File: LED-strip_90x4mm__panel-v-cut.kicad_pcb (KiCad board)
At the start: 2 copper layers, 99 x 100 mm, 774 parts, among them P1 CONN_2, P10 CONN_2, P11 CONN_2, P12 CONN_2, P2 CONN_2, P3 CONN_2, P4 CONN_2, P5 CONN_2, P6 CONN_2, P7 CONN_2, P8 CONN_2, P9 CONN_2

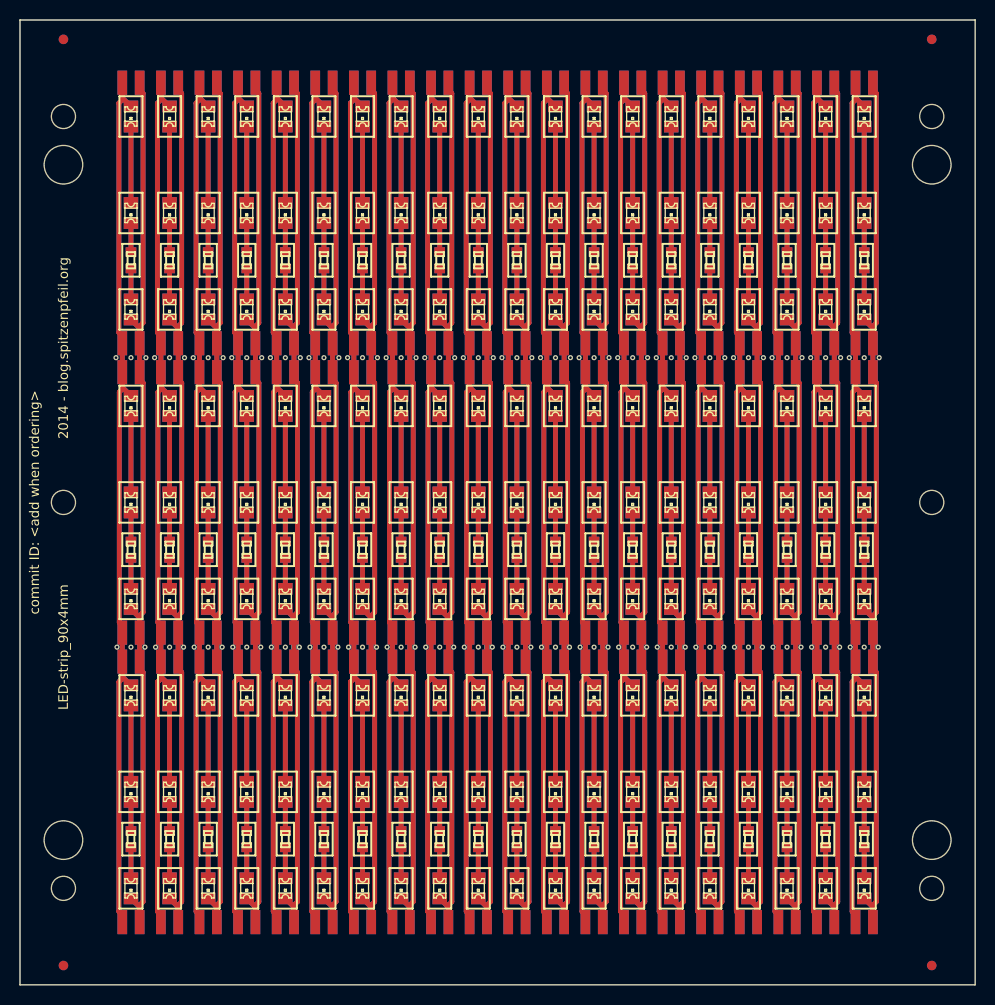
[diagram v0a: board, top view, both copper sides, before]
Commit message: Removed fiducials + alignment holes from panel --> 20% more boards.
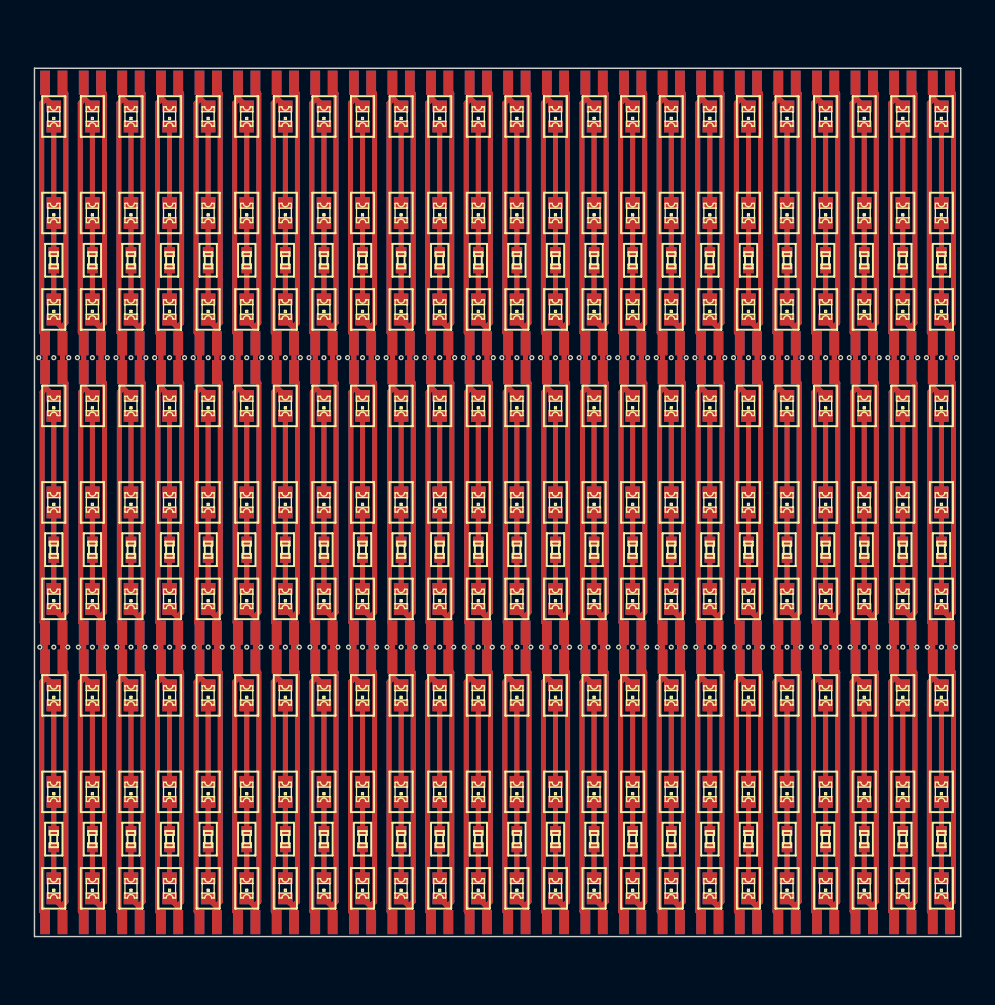
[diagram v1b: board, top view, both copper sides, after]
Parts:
- removed 1PIN (x4): P***, 1pin
- removed BH1: BH1, 1pin
- removed BH2: BH2, 1pin
- removed BH3: BH3, 1pin
- removed BH4: BH4, 1pin
- removed SM1: SM1, 1pin
- removed SM2: SM2, 1pin
- removed SM3: SM3, 1pin
- removed SM4: SM4, 1pin
- removed SM5: SM5, 1pin
- removed SM6: SM6, 1pin
- added D1: LED, my_parts:MADW__CHIPLED-0805, F.Cu at (288.5, 153.0)
- added D1: LED, my_parts:MADW__CHIPLED-0805, F.Cu at (284.5, 153.0)
- added D1: LED, my_parts:MADW__CHIPLED-0805, F.Cu at (372.5, 153.0)
- added D1: LED, my_parts:MADW__CHIPLED-0805, F.Cu at (376.5, 153.0)
- added D10: LED, my_parts:MADW__CHIPLED-0805, B.Cu at (288.5, 93.0)
- added D10: LED, my_parts:MADW__CHIPLED-0805, B.Cu at (284.5, 93.0)
- added D10: LED, my_parts:MADW__CHIPLED-0805, B.Cu at (372.5, 93.0)
- added D10: LED, my_parts:MADW__CHIPLED-0805, B.Cu at (376.5, 93.0)
- added D11: LED, my_parts:MADW__CHIPLED-0805, B.Cu at (288.5, 103.0)
- added D11: LED, my_parts:MADW__CHIPLED-0805, B.Cu at (284.5, 103.0)
- added D11: LED, my_parts:MADW__CHIPLED-0805, B.Cu at (372.5, 103.0)
- added D11: LED, my_parts:MADW__CHIPLED-0805, B.Cu at (376.5, 103.0)
- added D12: LED, my_parts:MADW__CHIPLED-0805, B.Cu at (288.5, 113.0)
- added D12: LED, my_parts:MADW__CHIPLED-0805, B.Cu at (284.5, 113.0)
- added D12: LED, my_parts:MADW__CHIPLED-0805, B.Cu at (372.5, 113.0)
- added D12: LED, my_parts:MADW__CHIPLED-0805, B.Cu at (376.5, 113.0)
- added D13: LED, my_parts:MADW__CHIPLED-0805, B.Cu at (288.5, 123.0)
- added D13: LED, my_parts:MADW__CHIPLED-0805, B.Cu at (284.5, 123.0)
- added D13: LED, my_parts:MADW__CHIPLED-0805, B.Cu at (372.5, 123.0)
- added D13: LED, my_parts:MADW__CHIPLED-0805, B.Cu at (376.5, 123.0)
- added D14: LED, my_parts:MADW__CHIPLED-0805, B.Cu at (288.5, 133.0)
- added D14: LED, my_parts:MADW__CHIPLED-0805, B.Cu at (284.5, 133.0)
- added D14: LED, my_parts:MADW__CHIPLED-0805, B.Cu at (372.5, 133.0)
- added D14: LED, my_parts:MADW__CHIPLED-0805, B.Cu at (376.5, 133.0)
- added D15: LED, my_parts:MADW__CHIPLED-0805, B.Cu at (288.5, 143.0)
- added D15: LED, my_parts:MADW__CHIPLED-0805, B.Cu at (284.5, 143.0)
- added D15: LED, my_parts:MADW__CHIPLED-0805, B.Cu at (372.5, 143.0)
- added D15: LED, my_parts:MADW__CHIPLED-0805, B.Cu at (376.5, 143.0)
- added D16: LED, my_parts:MADW__CHIPLED-0805, B.Cu at (288.5, 153.0)
- added D16: LED, my_parts:MADW__CHIPLED-0805, B.Cu at (284.5, 153.0)
- added D16: LED, my_parts:MADW__CHIPLED-0805, B.Cu at (372.5, 153.0)
- added D16: LED, my_parts:MADW__CHIPLED-0805, B.Cu at (376.5, 153.0)
- added D17: LED, my_parts:MADW__CHIPLED-0805, B.Cu at (288.5, 163.0)
- added D17: LED, my_parts:MADW__CHIPLED-0805, B.Cu at (284.5, 163.0)
- added D17: LED, my_parts:MADW__CHIPLED-0805, B.Cu at (372.5, 163.0)
- added D17: LED, my_parts:MADW__CHIPLED-0805, B.Cu at (376.5, 163.0)
- added D18: LED, my_parts:MADW__CHIPLED-0805, B.Cu at (288.5, 173.0)
- added D18: LED, my_parts:MADW__CHIPLED-0805, B.Cu at (284.5, 173.0)
- added D18: LED, my_parts:MADW__CHIPLED-0805, B.Cu at (372.5, 173.0)
- added D18: LED, my_parts:MADW__CHIPLED-0805, B.Cu at (376.5, 173.0)
- added D2: LED, my_parts:MADW__CHIPLED-0805, F.Cu at (288.5, 163.0)
- added D2: LED, my_parts:MADW__CHIPLED-0805, F.Cu at (284.5, 163.0)
- added D2: LED, my_parts:MADW__CHIPLED-0805, F.Cu at (372.5, 163.0)
- added D2: LED, my_parts:MADW__CHIPLED-0805, F.Cu at (376.5, 163.0)
- added D3: LED, my_parts:MADW__CHIPLED-0805, F.Cu at (288.5, 173.0)
- added D3: LED, my_parts:MADW__CHIPLED-0805, F.Cu at (284.5, 173.0)
- added D3: LED, my_parts:MADW__CHIPLED-0805, F.Cu at (372.5, 173.0)
- added D3: LED, my_parts:MADW__CHIPLED-0805, F.Cu at (376.5, 173.0)
- added D4: LED, my_parts:MADW__CHIPLED-0805, F.Cu at (288.5, 123.0)
- added D4: LED, my_parts:MADW__CHIPLED-0805, F.Cu at (284.5, 123.0)
- added D4: LED, my_parts:MADW__CHIPLED-0805, F.Cu at (372.5, 123.0)
- added D4: LED, my_parts:MADW__CHIPLED-0805, F.Cu at (376.5, 123.0)
- added D5: LED, my_parts:MADW__CHIPLED-0805, F.Cu at (288.5, 133.0)
- added D5: LED, my_parts:MADW__CHIPLED-0805, F.Cu at (284.5, 133.0)
- added D5: LED, my_parts:MADW__CHIPLED-0805, F.Cu at (372.5, 133.0)
- added D5: LED, my_parts:MADW__CHIPLED-0805, F.Cu at (376.5, 133.0)
- added D6: LED, my_parts:MADW__CHIPLED-0805, F.Cu at (288.5, 143.0)
- added D6: LED, my_parts:MADW__CHIPLED-0805, F.Cu at (284.5, 143.0)
- added D6: LED, my_parts:MADW__CHIPLED-0805, F.Cu at (372.5, 143.0)
- added D6: LED, my_parts:MADW__CHIPLED-0805, F.Cu at (376.5, 143.0)
- added D7: LED, my_parts:MADW__CHIPLED-0805, F.Cu at (288.5, 93.0)
- added D7: LED, my_parts:MADW__CHIPLED-0805, F.Cu at (284.5, 93.0)
- added D7: LED, my_parts:MADW__CHIPLED-0805, F.Cu at (372.5, 93.0)
- added D7: LED, my_parts:MADW__CHIPLED-0805, F.Cu at (376.5, 93.0)
- added D8: LED, my_parts:MADW__CHIPLED-0805, F.Cu at (288.5, 103.0)
- added D8: LED, my_parts:MADW__CHIPLED-0805, F.Cu at (284.5, 103.0)
- added D8: LED, my_parts:MADW__CHIPLED-0805, F.Cu at (372.5, 103.0)
- added D8: LED, my_parts:MADW__CHIPLED-0805, F.Cu at (376.5, 103.0)
- added D9: LED, my_parts:MADW__CHIPLED-0805, F.Cu at (288.5, 113.0)
- added D9: LED, my_parts:MADW__CHIPLED-0805, F.Cu at (284.5, 113.0)
- added D9: LED, my_parts:MADW__CHIPLED-0805, F.Cu at (372.5, 113.0)
- added D9: LED, my_parts:MADW__CHIPLED-0805, F.Cu at (376.5, 113.0)
- added G1: LED_smile_silkscreen_3mm, led-smile:LED_smile_silkscreen_3mm, B.Cu at (288.6, 98.1)
- added G1: LED_smile_silkscreen_3mm, led-smile:LED_smile_silkscreen_3mm, B.Cu at (284.6, 98.1)
- added G1: LED_smile_silkscreen_3mm, led-smile:LED_smile_silkscreen_3mm, B.Cu at (372.6, 98.1)
- added G1: LED_smile_silkscreen_3mm, led-smile:LED_smile_silkscreen_3mm, B.Cu at (376.6, 98.1)
- added G2: OSHW-logo_silkscreen_3mm, oshw-logo:OSHW-logo_silkscreen_3mm, B.Cu at (288.5, 128.1)
- added G2: OSHW-logo_silkscreen_3mm, oshw-logo:OSHW-logo_silkscreen_3mm, B.Cu at (284.5, 128.1)
- added G2: OSHW-logo_silkscreen_3mm, oshw-logo:OSHW-logo_silkscreen_3mm, B.Cu at (372.5, 128.1)
- added G2: OSHW-logo_silkscreen_3mm, oshw-logo:OSHW-logo_silkscreen_3mm, B.Cu at (376.5, 128.1)
- added P1: CONN_2, my_parts:MADW__SIL-2, F.Cu at (288.5, 176.5)
- added P1: CONN_2, my_parts:MADW__SIL-2, F.Cu at (284.5, 176.5)
- added P1: CONN_2, my_parts:MADW__SIL-2, F.Cu at (372.5, 176.5)
- added P1: CONN_2, my_parts:MADW__SIL-2, F.Cu at (376.5, 176.5)
- added P10: CONN_2, my_parts:MADW__SIL-2, B.Cu at (288.5, 146.5)
- added P10: CONN_2, my_parts:MADW__SIL-2, B.Cu at (284.5, 146.5)
- added P10: CONN_2, my_parts:MADW__SIL-2, B.Cu at (372.5, 146.5)
- added P10: CONN_2, my_parts:MADW__SIL-2, B.Cu at (376.5, 146.5)
- added P11: CONN_2, my_parts:MADW__SIL-2, B.Cu at (288.5, 149.5)
- added P11: CONN_2, my_parts:MADW__SIL-2, B.Cu at (284.5, 149.5)
- added P11: CONN_2, my_parts:MADW__SIL-2, B.Cu at (372.5, 149.5)
- added P11: CONN_2, my_parts:MADW__SIL-2, B.Cu at (376.5, 149.5)
- added P12: CONN_2, my_parts:MADW__SIL-2, B.Cu at (288.5, 176.5)
- added P12: CONN_2, my_parts:MADW__SIL-2, B.Cu at (284.5, 176.5)
- added P12: CONN_2, my_parts:MADW__SIL-2, B.Cu at (372.5, 176.5)
- added P12: CONN_2, my_parts:MADW__SIL-2, B.Cu at (376.5, 176.5)
- added P2: CONN_2, my_parts:MADW__SIL-2, F.Cu at (288.5, 149.5)
- added P2: CONN_2, my_parts:MADW__SIL-2, F.Cu at (284.5, 149.5)
- added P2: CONN_2, my_parts:MADW__SIL-2, F.Cu at (372.5, 149.5)
- added P2: CONN_2, my_parts:MADW__SIL-2, F.Cu at (376.5, 149.5)
- added P3: CONN_2, my_parts:MADW__SIL-2, F.Cu at (288.5, 146.5)
- added P3: CONN_2, my_parts:MADW__SIL-2, F.Cu at (284.5, 146.5)
- added P3: CONN_2, my_parts:MADW__SIL-2, F.Cu at (372.5, 146.5)
- added P3: CONN_2, my_parts:MADW__SIL-2, F.Cu at (376.5, 146.5)
- added P4: CONN_2, my_parts:MADW__SIL-2, F.Cu at (288.5, 119.5)
- added P4: CONN_2, my_parts:MADW__SIL-2, F.Cu at (284.5, 119.5)
- added P4: CONN_2, my_parts:MADW__SIL-2, F.Cu at (372.5, 119.5)
- added P4: CONN_2, my_parts:MADW__SIL-2, F.Cu at (376.5, 119.5)
- added P5: CONN_2, my_parts:MADW__SIL-2, F.Cu at (288.5, 116.5)
- added P5: CONN_2, my_parts:MADW__SIL-2, F.Cu at (284.5, 116.5)
- added P5: CONN_2, my_parts:MADW__SIL-2, F.Cu at (372.5, 116.5)
- added P5: CONN_2, my_parts:MADW__SIL-2, F.Cu at (376.5, 116.5)
- added P6: CONN_2, my_parts:MADW__SIL-2, F.Cu at (288.5, 89.5)
- added P6: CONN_2, my_parts:MADW__SIL-2, F.Cu at (284.5, 89.5)
- added P6: CONN_2, my_parts:MADW__SIL-2, F.Cu at (372.5, 89.5)
- added P6: CONN_2, my_parts:MADW__SIL-2, F.Cu at (376.5, 89.5)
- added P7: CONN_2, my_parts:MADW__SIL-2, B.Cu at (288.5, 89.5)
- added P7: CONN_2, my_parts:MADW__SIL-2, B.Cu at (284.5, 89.5)
- added P7: CONN_2, my_parts:MADW__SIL-2, B.Cu at (372.5, 89.5)
- added P7: CONN_2, my_parts:MADW__SIL-2, B.Cu at (376.5, 89.5)
- added P8: CONN_2, my_parts:MADW__SIL-2, B.Cu at (288.5, 116.5)
- added P8: CONN_2, my_parts:MADW__SIL-2, B.Cu at (284.5, 116.5)
- added P8: CONN_2, my_parts:MADW__SIL-2, B.Cu at (372.5, 116.5)
- added P8: CONN_2, my_parts:MADW__SIL-2, B.Cu at (376.5, 116.5)
- added P9: CONN_2, my_parts:MADW__SIL-2, B.Cu at (288.5, 119.5)
- added P9: CONN_2, my_parts:MADW__SIL-2, B.Cu at (284.5, 119.5)
- added P9: CONN_2, my_parts:MADW__SIL-2, B.Cu at (372.5, 119.5)
- added P9: CONN_2, my_parts:MADW__SIL-2, B.Cu at (376.5, 119.5)
- added R1: R, my_parts:MADW__R0603_2, F.Cu at (288.5, 167.9)
- added R1: R, my_parts:MADW__R0603_2, F.Cu at (284.5, 167.9)
- added R1: R, my_parts:MADW__R0603_2, F.Cu at (372.5, 167.9)
- added R1: R, my_parts:MADW__R0603_2, F.Cu at (376.5, 167.9)
- added R2: R, my_parts:MADW__R0603_2, F.Cu at (288.5, 137.9)
- added R2: R, my_parts:MADW__R0603_2, F.Cu at (284.5, 137.9)
- added R2: R, my_parts:MADW__R0603_2, F.Cu at (372.5, 137.9)
- added R2: R, my_parts:MADW__R0603_2, F.Cu at (376.5, 137.9)
- added R3: R, my_parts:MADW__R0603_2, F.Cu at (288.5, 107.9)
- added R3: R, my_parts:MADW__R0603_2, F.Cu at (284.5, 107.9)
- added R3: R, my_parts:MADW__R0603_2, F.Cu at (372.5, 107.9)
- added R3: R, my_parts:MADW__R0603_2, F.Cu at (376.5, 107.9)
- added R4: R, my_parts:MADW__R0603_2, B.Cu at (288.5, 107.9)
- added R4: R, my_parts:MADW__R0603_2, B.Cu at (284.5, 107.9)
- added R4: R, my_parts:MADW__R0603_2, B.Cu at (372.5, 107.9)
- added R4: R, my_parts:MADW__R0603_2, B.Cu at (376.5, 107.9)
- added R5: R, my_parts:MADW__R0603_2, B.Cu at (288.5, 137.9)
- added R5: R, my_parts:MADW__R0603_2, B.Cu at (284.5, 137.9)
- added R5: R, my_parts:MADW__R0603_2, B.Cu at (372.5, 137.9)
- added R5: R, my_parts:MADW__R0603_2, B.Cu at (376.5, 137.9)
- added R6: R, my_parts:MADW__R0603_2, B.Cu at (288.5, 167.9)
- added R6: R, my_parts:MADW__R0603_2, B.Cu at (284.5, 167.9)
- added R6: R, my_parts:MADW__R0603_2, B.Cu at (372.5, 167.9)
- added R6: R, my_parts:MADW__R0603_2, B.Cu at (376.5, 167.9)
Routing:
- net /GND: track 3916.7 -> 4700.1 mm
- net /VCC: track 3876.0 -> 4651.3 mm
- net Net-(D7-Pad2): track 158.0 -> 189.6 mm
- net Net-(D10-Pad2): track 158.0 -> 189.6 mm
- net Net-(D4-Pad2): track 158.0 -> 189.6 mm
- net Net-(D16-Pad2): track 158.0 -> 189.6 mm
- net Net-(D13-Pad2): track 158.0 -> 189.6 mm
- net Net-(D1-Pad2): track 158.0 -> 189.6 mm
- net Net-(D9-Pad1): track 64.1 -> 76.9 mm
- net Net-(D6-Pad1): track 64.1 -> 76.9 mm
- net Net-(D3-Pad1): track 64.1 -> 76.9 mm
- net Net-(D18-Pad1): track 64.1 -> 76.9 mm
- net Net-(D15-Pad1): track 64.1 -> 76.9 mm
- net Net-(D12-Pad1): track 64.1 -> 76.9 mm
- net Net-(D8-Pad2): track 60.1 -> 72.1 mm
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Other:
- board size 99 x 100 mm -> 96 x 90 mm
- board text removed: "2014 - blog.spitzenpfeil.org"
- board text removed: "LED-strip_90x4mm"
- board text removed: "commit ID: <add when ordering>"

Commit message: Redid the panel.
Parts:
- removed the D1 at (288.5, 153.0)
- removed the D1 at (328.5, 153.0)
- removed the D1 at (312.5, 153.0)
- removed the D1 at (316.5, 153.0)
- removed the D1 at (324.5, 153.0)
- removed the D1 at (320.5, 153.0)
- removed the D1 at (360.5, 153.0)
- removed the D1 at (364.5, 153.0)
- removed the D1 at (356.5, 153.0)
- removed the D1 at (352.5, 153.0)
- removed the D1 at (368.5, 153.0)
- removed the D1 at (284.5, 153.0)
- removed the D1 at (348.5, 153.0)
- removed the D1 at (332.5, 153.0)
- removed the D1 at (336.5, 153.0)
- removed the D1 at (344.5, 153.0)
- removed the D1 at (340.5, 153.0)
- removed the D1 at (372.5, 153.0)
- removed the D1 at (376.5, 153.0)
- removed the D1 at (300.5, 153.0)
- removed the D1 at (304.5, 153.0)
- removed the D1 at (296.5, 153.0)
- removed the D1 at (292.5, 153.0)
- removed the D1 at (308.5, 153.0)
- removed the D10 at (288.5, 93.0)
- removed the D10 at (328.5, 93.0)
- removed the D10 at (312.5, 93.0)
- removed the D10 at (316.5, 93.0)
- removed the D10 at (324.5, 93.0)
- removed the D10 at (320.5, 93.0)
- removed the D10 at (360.5, 93.0)
- removed the D10 at (364.5, 93.0)
- removed the D10 at (356.5, 93.0)
- removed the D10 at (352.5, 93.0)
- removed the D10 at (368.5, 93.0)
- removed the D10 at (284.5, 93.0)
- removed the D10 at (348.5, 93.0)
- removed the D10 at (332.5, 93.0)
- removed the D10 at (336.5, 93.0)
- removed the D10 at (344.5, 93.0)
- removed the D10 at (340.5, 93.0)
- removed the D10 at (372.5, 93.0)
- removed the D10 at (376.5, 93.0)
- removed the D10 at (300.5, 93.0)
- removed the D10 at (304.5, 93.0)
- removed the D10 at (296.5, 93.0)
- removed the D10 at (292.5, 93.0)
- removed the D10 at (308.5, 93.0)
- removed the D11 at (288.5, 103.0)
- removed the D11 at (328.5, 103.0)
- removed the D11 at (312.5, 103.0)
- removed the D11 at (316.5, 103.0)
- removed the D11 at (324.5, 103.0)
- removed the D11 at (320.5, 103.0)
- removed the D11 at (360.5, 103.0)
- removed the D11 at (364.5, 103.0)
- removed the D11 at (356.5, 103.0)
- removed the D11 at (352.5, 103.0)
- removed the D11 at (368.5, 103.0)
- removed the D11 at (284.5, 103.0)
- removed the D11 at (348.5, 103.0)
- removed the D11 at (332.5, 103.0)
- removed the D11 at (336.5, 103.0)
- removed the D11 at (344.5, 103.0)
- removed the D11 at (340.5, 103.0)
- removed the D11 at (372.5, 103.0)
- removed the D11 at (376.5, 103.0)
- removed the D11 at (300.5, 103.0)
- removed the D11 at (304.5, 103.0)
- removed the D11 at (296.5, 103.0)
- removed the D11 at (292.5, 103.0)
- removed the D11 at (308.5, 103.0)
- removed the D12 at (288.5, 113.0)
- removed the D12 at (328.5, 113.0)
- removed the D12 at (312.5, 113.0)
- removed the D12 at (316.5, 113.0)
- removed the D12 at (324.5, 113.0)
- removed the D12 at (320.5, 113.0)
- removed the D12 at (360.5, 113.0)
- removed the D12 at (364.5, 113.0)
- removed the D12 at (356.5, 113.0)
- removed the D12 at (352.5, 113.0)
- removed the D12 at (368.5, 113.0)
- removed the D12 at (284.5, 113.0)
- removed the D12 at (348.5, 113.0)
- removed the D12 at (332.5, 113.0)
- removed the D12 at (336.5, 113.0)
- removed the D12 at (344.5, 113.0)
- removed the D12 at (340.5, 113.0)
- removed the D12 at (372.5, 113.0)
- removed the D12 at (376.5, 113.0)
- removed the D12 at (300.5, 113.0)
- removed the D12 at (304.5, 113.0)
- removed the D12 at (296.5, 113.0)
- removed the D12 at (292.5, 113.0)
- removed the D12 at (308.5, 113.0)
- removed the D13 at (288.5, 123.0)
- removed the D13 at (328.5, 123.0)
- removed the D13 at (312.5, 123.0)
- removed the D13 at (316.5, 123.0)
- removed the D13 at (324.5, 123.0)
- removed the D13 at (320.5, 123.0)
- removed the D13 at (360.5, 123.0)
- removed the D13 at (364.5, 123.0)
- removed the D13 at (356.5, 123.0)
- removed the D13 at (352.5, 123.0)
- removed the D13 at (368.5, 123.0)
- removed the D13 at (284.5, 123.0)
- removed the D13 at (348.5, 123.0)
- removed the D13 at (332.5, 123.0)
- removed the D13 at (336.5, 123.0)
- removed the D13 at (344.5, 123.0)
- removed the D13 at (340.5, 123.0)
- removed the D13 at (372.5, 123.0)
- removed the D13 at (376.5, 123.0)
- removed the D13 at (300.5, 123.0)
- removed the D13 at (304.5, 123.0)
- removed the D13 at (296.5, 123.0)
- removed the D13 at (292.5, 123.0)
- removed the D13 at (308.5, 123.0)
- removed the D14 at (288.5, 133.0)
- removed the D14 at (328.5, 133.0)
- removed the D14 at (312.5, 133.0)
- removed the D14 at (316.5, 133.0)
- removed the D14 at (324.5, 133.0)
- removed the D14 at (320.5, 133.0)
- removed the D14 at (360.5, 133.0)
- removed the D14 at (364.5, 133.0)
- removed the D14 at (356.5, 133.0)
- removed the D14 at (352.5, 133.0)
- removed the D14 at (368.5, 133.0)
- removed the D14 at (284.5, 133.0)
- removed the D14 at (348.5, 133.0)
- removed the D14 at (332.5, 133.0)
- removed the D14 at (336.5, 133.0)
- removed the D14 at (344.5, 133.0)
- removed the D14 at (340.5, 133.0)
- removed the D14 at (372.5, 133.0)
- removed the D14 at (376.5, 133.0)
- removed the D14 at (300.5, 133.0)
- removed the D14 at (304.5, 133.0)
- removed the D14 at (296.5, 133.0)
- removed the D14 at (292.5, 133.0)
- removed the D14 at (308.5, 133.0)
- removed the D15 at (288.5, 143.0)
- removed the D15 at (328.5, 143.0)
- removed the D15 at (312.5, 143.0)
- removed the D15 at (316.5, 143.0)
- removed the D15 at (324.5, 143.0)
- removed the D15 at (320.5, 143.0)
- removed the D15 at (360.5, 143.0)
- removed the D15 at (364.5, 143.0)
- removed the D15 at (356.5, 143.0)
- removed the D15 at (352.5, 143.0)
- removed the D15 at (368.5, 143.0)
- removed the D15 at (284.5, 143.0)
- removed the D15 at (348.5, 143.0)
- removed the D15 at (332.5, 143.0)
- removed the D15 at (336.5, 143.0)
- removed the D15 at (344.5, 143.0)
- removed the D15 at (340.5, 143.0)
- removed the D15 at (372.5, 143.0)
- removed the D15 at (376.5, 143.0)
- removed the D15 at (300.5, 143.0)
- removed the D15 at (304.5, 143.0)
- removed the D15 at (296.5, 143.0)
- removed the D15 at (292.5, 143.0)
- removed the D15 at (308.5, 143.0)
- removed the D16 at (288.5, 153.0)
- removed the D16 at (328.5, 153.0)
- removed the D16 at (312.5, 153.0)
- removed the D16 at (316.5, 153.0)
- removed the D16 at (324.5, 153.0)
- removed the D16 at (320.5, 153.0)
- removed the D16 at (360.5, 153.0)
- removed the D16 at (364.5, 153.0)
- removed the D16 at (356.5, 153.0)
- removed the D16 at (352.5, 153.0)
- removed the D16 at (368.5, 153.0)
- removed the D16 at (284.5, 153.0)
- removed the D16 at (348.5, 153.0)
- removed the D16 at (332.5, 153.0)
- removed the D16 at (336.5, 153.0)
- removed the D16 at (344.5, 153.0)
- removed the D16 at (340.5, 153.0)
- removed the D16 at (372.5, 153.0)
- removed the D16 at (376.5, 153.0)
- removed the D16 at (300.5, 153.0)
- removed the D16 at (304.5, 153.0)
- removed the D16 at (296.5, 153.0)
- removed the D16 at (292.5, 153.0)
- removed the D16 at (308.5, 153.0)
- removed the D17 at (288.5, 163.0)
- removed the D17 at (328.5, 163.0)
- removed the D17 at (312.5, 163.0)
- removed the D17 at (316.5, 163.0)
- removed the D17 at (324.5, 163.0)
- removed the D17 at (320.5, 163.0)
- removed the D17 at (360.5, 163.0)
- removed the D17 at (364.5, 163.0)
- removed the D17 at (356.5, 163.0)
- removed the D17 at (352.5, 163.0)
- removed the D17 at (368.5, 163.0)
- removed the D17 at (284.5, 163.0)
- removed the D17 at (348.5, 163.0)
- removed the D17 at (332.5, 163.0)
- removed the D17 at (336.5, 163.0)
- removed the D17 at (344.5, 163.0)
- removed the D17 at (340.5, 163.0)
- removed the D17 at (372.5, 163.0)
- removed the D17 at (376.5, 163.0)
- removed the D17 at (300.5, 163.0)
- removed the D17 at (304.5, 163.0)
- removed the D17 at (296.5, 163.0)
- removed the D17 at (292.5, 163.0)
- removed the D17 at (308.5, 163.0)
- removed the D18 at (288.5, 173.0)
- removed the D18 at (328.5, 173.0)
- removed the D18 at (312.5, 173.0)
- removed the D18 at (316.5, 173.0)
- removed the D18 at (324.5, 173.0)
- removed the D18 at (320.5, 173.0)
- removed the D18 at (360.5, 173.0)
- removed the D18 at (364.5, 173.0)
- removed the D18 at (356.5, 173.0)
- removed the D18 at (352.5, 173.0)
- removed the D18 at (368.5, 173.0)
- removed the D18 at (284.5, 173.0)
- removed the D18 at (348.5, 173.0)
- removed the D18 at (332.5, 173.0)
- removed the D18 at (336.5, 173.0)
- removed the D18 at (344.5, 173.0)
- removed the D18 at (340.5, 173.0)
- removed the D18 at (372.5, 173.0)
- removed the D18 at (376.5, 173.0)
- removed the D18 at (300.5, 173.0)
- removed the D18 at (304.5, 173.0)
- removed the D18 at (296.5, 173.0)
- removed the D18 at (292.5, 173.0)
- removed the D18 at (308.5, 173.0)
- removed the D2 at (288.5, 163.0)
- removed the D2 at (328.5, 163.0)
- removed the D2 at (312.5, 163.0)
- removed the D2 at (316.5, 163.0)
- removed the D2 at (324.5, 163.0)
- removed the D2 at (320.5, 163.0)
- removed the D2 at (360.5, 163.0)
- removed the D2 at (364.5, 163.0)
- removed the D2 at (356.5, 163.0)
- removed the D2 at (352.5, 163.0)
- removed the D2 at (368.5, 163.0)
- removed the D2 at (284.5, 163.0)
- removed the D2 at (348.5, 163.0)
- removed the D2 at (332.5, 163.0)
- removed the D2 at (336.5, 163.0)
- removed the D2 at (344.5, 163.0)
- removed the D2 at (340.5, 163.0)
- removed the D2 at (372.5, 163.0)
- removed the D2 at (376.5, 163.0)
- removed the D2 at (300.5, 163.0)
- removed the D2 at (304.5, 163.0)
- removed the D2 at (296.5, 163.0)
- removed the D2 at (292.5, 163.0)
- removed the D2 at (308.5, 163.0)
- removed the D3 at (288.5, 173.0)
- removed the D3 at (328.5, 173.0)
- removed the D3 at (312.5, 173.0)
- removed the D3 at (316.5, 173.0)
- removed the D3 at (324.5, 173.0)
- removed the D3 at (320.5, 173.0)
- removed the D3 at (360.5, 173.0)
- removed the D3 at (364.5, 173.0)
- removed the D3 at (356.5, 173.0)
- removed the D3 at (352.5, 173.0)
- removed the D3 at (368.5, 173.0)
- removed the D3 at (284.5, 173.0)
- removed the D3 at (348.5, 173.0)
- removed the D3 at (332.5, 173.0)
- removed the D3 at (336.5, 173.0)
- removed the D3 at (344.5, 173.0)
- removed the D3 at (340.5, 173.0)
- removed the D3 at (372.5, 173.0)
- removed the D3 at (376.5, 173.0)
- removed the D3 at (300.5, 173.0)
- removed the D3 at (304.5, 173.0)
- removed the D3 at (296.5, 173.0)
- removed the D3 at (292.5, 173.0)
- removed the D3 at (308.5, 173.0)
- removed the D4 at (288.5, 123.0)
- removed the D4 at (328.5, 123.0)
- removed the D4 at (312.5, 123.0)
- removed the D4 at (316.5, 123.0)
- removed the D4 at (324.5, 123.0)
- removed the D4 at (320.5, 123.0)
- removed the D4 at (360.5, 123.0)
- removed the D4 at (364.5, 123.0)
- removed the D4 at (356.5, 123.0)
- removed the D4 at (352.5, 123.0)
- removed the D4 at (368.5, 123.0)
- removed the D4 at (284.5, 123.0)
- removed the D4 at (348.5, 123.0)
- removed the D4 at (332.5, 123.0)
- removed the D4 at (336.5, 123.0)
- removed the D4 at (344.5, 123.0)
- removed the D4 at (340.5, 123.0)
- removed the D4 at (372.5, 123.0)
- removed the D4 at (376.5, 123.0)
- removed the D4 at (300.5, 123.0)
- removed the D4 at (304.5, 123.0)
- removed the D4 at (296.5, 123.0)
- removed the D4 at (292.5, 123.0)
- removed the D4 at (308.5, 123.0)
- removed the D5 at (288.5, 133.0)
- removed the D5 at (328.5, 133.0)
- removed the D5 at (312.5, 133.0)
- removed the D5 at (316.5, 133.0)
- removed the D5 at (324.5, 133.0)
- removed the D5 at (320.5, 133.0)
- removed the D5 at (360.5, 133.0)
- removed the D5 at (364.5, 133.0)
- removed the D5 at (356.5, 133.0)
- removed the D5 at (352.5, 133.0)
- removed the D5 at (368.5, 133.0)
- removed the D5 at (284.5, 133.0)
- removed the D5 at (348.5, 133.0)
- removed the D5 at (332.5, 133.0)
- removed the D5 at (336.5, 133.0)
- removed the D5 at (344.5, 133.0)
- removed the D5 at (340.5, 133.0)
- removed the D5 at (372.5, 133.0)
- removed the D5 at (376.5, 133.0)
- removed the D5 at (300.5, 133.0)
- removed the D5 at (304.5, 133.0)
- removed the D5 at (296.5, 133.0)
- removed the D5 at (292.5, 133.0)
- removed the D5 at (308.5, 133.0)
- removed the D6 at (288.5, 143.0)
- removed the D6 at (328.5, 143.0)
- removed the D6 at (312.5, 143.0)
- removed the D6 at (316.5, 143.0)
- removed the D6 at (324.5, 143.0)
- removed the D6 at (320.5, 143.0)
- removed the D6 at (360.5, 143.0)
- removed the D6 at (364.5, 143.0)
- removed the D6 at (356.5, 143.0)
- removed the D6 at (352.5, 143.0)
- removed the D6 at (368.5, 143.0)
- removed the D6 at (284.5, 143.0)
- removed the D6 at (348.5, 143.0)
- removed the D6 at (332.5, 143.0)
- removed the D6 at (336.5, 143.0)
- removed the D6 at (344.5, 143.0)
- removed the D6 at (340.5, 143.0)
- removed the D6 at (372.5, 143.0)
- removed the D6 at (376.5, 143.0)
- removed the D6 at (300.5, 143.0)
- removed the D6 at (304.5, 143.0)
- removed the D6 at (296.5, 143.0)
- removed the D6 at (292.5, 143.0)
- removed the D6 at (308.5, 143.0)
- removed the D7 at (288.5, 93.0)
- removed the D7 at (328.5, 93.0)
- removed the D7 at (312.5, 93.0)
- removed the D7 at (316.5, 93.0)
- removed the D7 at (324.5, 93.0)
- removed the D7 at (320.5, 93.0)
- removed the D7 at (360.5, 93.0)
- removed the D7 at (364.5, 93.0)
- removed the D7 at (356.5, 93.0)
- removed the D7 at (352.5, 93.0)
- removed the D7 at (368.5, 93.0)
- removed the D7 at (284.5, 93.0)
- removed the D7 at (348.5, 93.0)
- removed the D7 at (332.5, 93.0)
- removed the D7 at (336.5, 93.0)
- removed the D7 at (344.5, 93.0)
- removed the D7 at (340.5, 93.0)
- removed the D7 at (372.5, 93.0)
- removed the D7 at (376.5, 93.0)
- removed the D7 at (300.5, 93.0)
- removed the D7 at (304.5, 93.0)
- removed the D7 at (296.5, 93.0)
- removed the D7 at (292.5, 93.0)
- removed the D7 at (308.5, 93.0)
- removed the D8 at (288.5, 103.0)
- removed the D8 at (328.5, 103.0)
- removed the D8 at (312.5, 103.0)
- removed the D8 at (316.5, 103.0)
- removed the D8 at (324.5, 103.0)
- removed the D8 at (320.5, 103.0)
- removed the D8 at (360.5, 103.0)
- removed the D8 at (364.5, 103.0)
- removed the D8 at (356.5, 103.0)
- removed the D8 at (352.5, 103.0)
- removed the D8 at (368.5, 103.0)
- removed the D8 at (284.5, 103.0)
- removed the D8 at (348.5, 103.0)
- removed the D8 at (332.5, 103.0)
- removed the D8 at (336.5, 103.0)
- removed the D8 at (344.5, 103.0)
- removed the D8 at (340.5, 103.0)
- removed the D8 at (372.5, 103.0)
- removed the D8 at (376.5, 103.0)
- removed the D8 at (300.5, 103.0)
- removed the D8 at (304.5, 103.0)
- removed the D8 at (296.5, 103.0)
- removed the D8 at (292.5, 103.0)
- removed the D8 at (308.5, 103.0)
- removed the D9 at (288.5, 113.0)
- removed the D9 at (328.5, 113.0)
- removed the D9 at (312.5, 113.0)
- removed the D9 at (316.5, 113.0)
- removed the D9 at (324.5, 113.0)
- removed the D9 at (320.5, 113.0)
- removed the D9 at (360.5, 113.0)
- removed the D9 at (364.5, 113.0)
- removed the D9 at (356.5, 113.0)
- removed the D9 at (352.5, 113.0)
- removed the D9 at (368.5, 113.0)
- removed the D9 at (284.5, 113.0)
- removed the D9 at (348.5, 113.0)
- removed the D9 at (332.5, 113.0)
- removed the D9 at (336.5, 113.0)
- removed the D9 at (344.5, 113.0)
- removed the D9 at (340.5, 113.0)
- removed the D9 at (372.5, 113.0)
- removed the D9 at (376.5, 113.0)
- removed the D9 at (300.5, 113.0)
- removed the D9 at (304.5, 113.0)
- removed the D9 at (296.5, 113.0)
- removed the D9 at (292.5, 113.0)
- removed the D9 at (308.5, 113.0)
- removed the G1 at (288.6, 98.1)
- removed the G1 at (328.6, 98.1)
- removed the G1 at (312.6, 98.1)
- removed the G1 at (316.6, 98.1)
- removed the G1 at (324.6, 98.1)
- removed the G1 at (320.6, 98.1)
- removed the G1 at (360.6, 98.1)
- removed the G1 at (364.6, 98.1)
- removed the G1 at (356.6, 98.1)
- removed the G1 at (352.6, 98.1)
- removed the G1 at (368.6, 98.1)
- removed the G1 at (284.6, 98.1)
- removed the G1 at (348.6, 98.1)
- removed the G1 at (332.6, 98.1)
- removed the G1 at (336.6, 98.1)
- removed the G1 at (344.6, 98.1)
- removed the G1 at (340.6, 98.1)
- removed the G1 at (372.6, 98.1)
- removed the G1 at (376.6, 98.1)
- removed the G1 at (300.6, 98.1)
- removed the G1 at (304.6, 98.1)
- removed the G1 at (296.6, 98.1)
- removed the G1 at (292.6, 98.1)
- removed the G1 at (308.6, 98.1)
- removed the G2 at (288.5, 128.1)
- removed the G2 at (328.5, 128.1)
- removed the G2 at (312.5, 128.1)
- removed the G2 at (316.5, 128.1)
- removed the G2 at (324.5, 128.1)
- removed the G2 at (320.5, 128.1)
- removed the G2 at (360.5, 128.1)
- removed the G2 at (364.5, 128.1)
- removed the G2 at (356.5, 128.1)
- removed the G2 at (352.5, 128.1)
- removed the G2 at (368.5, 128.1)
- removed the G2 at (284.5, 128.1)
- removed the G2 at (348.5, 128.1)
- removed the G2 at (332.5, 128.1)
- removed the G2 at (336.5, 128.1)
- removed the G2 at (344.5, 128.1)
- removed the G2 at (340.5, 128.1)
- removed the G2 at (372.5, 128.1)
- removed the G2 at (376.5, 128.1)
- removed the G2 at (300.5, 128.1)
- removed the G2 at (304.5, 128.1)
- removed the G2 at (296.5, 128.1)
- removed the G2 at (292.5, 128.1)
- removed the G2 at (308.5, 128.1)
- removed the P1 at (288.5, 176.5)
- removed the P1 at (328.5, 176.5)
- removed the P1 at (312.5, 176.5)
- removed the P1 at (316.5, 176.5)
- removed the P1 at (324.5, 176.5)
- removed the P1 at (320.5, 176.5)
- removed the P1 at (360.5, 176.5)
- removed the P1 at (364.5, 176.5)
- removed the P1 at (356.5, 176.5)
- removed the P1 at (352.5, 176.5)
- removed the P1 at (368.5, 176.5)
- removed the P1 at (284.5, 176.5)
- removed the P1 at (348.5, 176.5)
- removed the P1 at (332.5, 176.5)
- removed the P1 at (336.5, 176.5)
- removed the P1 at (344.5, 176.5)
- removed the P1 at (340.5, 176.5)
- removed the P1 at (372.5, 176.5)
- removed the P1 at (376.5, 176.5)
- removed the P1 at (300.5, 176.5)
- removed the P1 at (304.5, 176.5)
- removed the P1 at (296.5, 176.5)
- removed the P1 at (292.5, 176.5)
- removed the P1 at (308.5, 176.5)
- removed the P10 at (288.5, 146.5)
- removed the P10 at (328.5, 146.5)
- removed the P10 at (312.5, 146.5)
- removed the P10 at (316.5, 146.5)
- removed the P10 at (324.5, 146.5)
- removed the P10 at (320.5, 146.5)
- removed the P10 at (360.5, 146.5)
- removed the P10 at (364.5, 146.5)
- removed the P10 at (356.5, 146.5)
- removed the P10 at (352.5, 146.5)
- removed the P10 at (368.5, 146.5)
- removed the P10 at (284.5, 146.5)
- removed the P10 at (348.5, 146.5)
- removed the P10 at (332.5, 146.5)
- removed the P10 at (336.5, 146.5)
- removed the P10 at (344.5, 146.5)
- removed the P10 at (340.5, 146.5)
- removed the P10 at (372.5, 146.5)
- removed the P10 at (376.5, 146.5)
- removed the P10 at (300.5, 146.5)
- removed the P10 at (304.5, 146.5)
- removed the P10 at (296.5, 146.5)
- removed the P10 at (292.5, 146.5)
- removed the P10 at (308.5, 146.5)
- removed the P11 at (288.5, 149.5)
- removed the P11 at (328.5, 149.5)
- removed the P11 at (312.5, 149.5)
- removed the P11 at (316.5, 149.5)
- removed the P11 at (324.5, 149.5)
- removed the P11 at (320.5, 149.5)
- removed the P11 at (360.5, 149.5)
- removed the P11 at (364.5, 149.5)
- removed the P11 at (356.5, 149.5)
- removed the P11 at (352.5, 149.5)
- removed the P11 at (368.5, 149.5)
- removed the P11 at (284.5, 149.5)
- removed the P11 at (348.5, 149.5)
- removed the P11 at (332.5, 149.5)
- removed the P11 at (336.5, 149.5)
- removed the P11 at (344.5, 149.5)
- removed the P11 at (340.5, 149.5)
- removed the P11 at (372.5, 149.5)
- removed the P11 at (376.5, 149.5)
- removed the P11 at (300.5, 149.5)
- removed the P11 at (304.5, 149.5)
- removed the P11 at (296.5, 149.5)
- removed the P11 at (292.5, 149.5)
- removed the P11 at (308.5, 149.5)
- removed the P12 at (288.5, 176.5)
- removed the P12 at (328.5, 176.5)
- removed the P12 at (312.5, 176.5)
- removed the P12 at (316.5, 176.5)
- removed the P12 at (324.5, 176.5)
- removed the P12 at (320.5, 176.5)
- removed the P12 at (360.5, 176.5)
- removed the P12 at (364.5, 176.5)
- removed the P12 at (356.5, 176.5)
- removed the P12 at (352.5, 176.5)
- removed the P12 at (368.5, 176.5)
- removed the P12 at (284.5, 176.5)
- removed the P12 at (348.5, 176.5)
- removed the P12 at (332.5, 176.5)
- removed the P12 at (336.5, 176.5)
- removed the P12 at (344.5, 176.5)
- removed the P12 at (340.5, 176.5)
- removed the P12 at (372.5, 176.5)
- removed the P12 at (376.5, 176.5)
- removed the P12 at (300.5, 176.5)
- removed the P12 at (304.5, 176.5)
- removed the P12 at (296.5, 176.5)
- removed the P12 at (292.5, 176.5)
- removed the P12 at (308.5, 176.5)
- removed the P2 at (288.5, 149.5)
- removed the P2 at (348.5, 149.5)
- removed the P2 at (344.5, 149.5)
- removed the P2 at (340.5, 149.5)
- removed the P2 at (336.5, 149.5)
- removed the P2 at (332.5, 149.5)
- removed the P2 at (328.5, 149.5)
- removed the P2 at (324.5, 149.5)
- removed the P2 at (320.5, 149.5)
- removed the P2 at (316.5, 149.5)
- removed the P2 at (312.5, 149.5)
- removed the P2 at (284.5, 149.5)
- removed the P2 at (308.5, 149.5)
- removed the P2 at (304.5, 149.5)
- removed the P2 at (300.5, 149.5)
- removed the P2 at (296.5, 149.5)
- removed the P2 at (292.5, 149.5)
- removed the P2 at (372.5, 149.5)
- removed the P2 at (376.5, 149.5)
- removed the P2 at (368.5, 149.5)
- removed the P2 at (364.5, 149.5)
- removed the P2 at (360.5, 149.5)
- removed the P2 at (356.5, 149.5)
- removed the P2 at (352.5, 149.5)
- removed the P3 at (288.5, 146.5)
- removed the P3 at (328.5, 146.5)
- removed the P3 at (312.5, 146.5)
- removed the P3 at (316.5, 146.5)
- removed the P3 at (324.5, 146.5)
- removed the P3 at (320.5, 146.5)
- removed the P3 at (360.5, 146.5)
- removed the P3 at (364.5, 146.5)
- removed the P3 at (356.5, 146.5)
- removed the P3 at (352.5, 146.5)
- removed the P3 at (368.5, 146.5)
- removed the P3 at (284.5, 146.5)
- removed the P3 at (348.5, 146.5)
- removed the P3 at (332.5, 146.5)
- removed the P3 at (336.5, 146.5)
- removed the P3 at (344.5, 146.5)
- removed the P3 at (340.5, 146.5)
- removed the P3 at (372.5, 146.5)
- removed the P3 at (376.5, 146.5)
- removed the P3 at (300.5, 146.5)
- removed the P3 at (304.5, 146.5)
- removed the P3 at (296.5, 146.5)
- removed the P3 at (292.5, 146.5)
- removed the P3 at (308.5, 146.5)
- removed the P4 at (288.5, 119.5)
- removed the P4 at (348.5, 119.5)
- removed the P4 at (344.5, 119.5)
- removed the P4 at (340.5, 119.5)
- removed the P4 at (336.5, 119.5)
- removed the P4 at (332.5, 119.5)
- removed the P4 at (328.5, 119.5)
- removed the P4 at (324.5, 119.5)
- removed the P4 at (320.5, 119.5)
- removed the P4 at (316.5, 119.5)
- removed the P4 at (312.5, 119.5)
- removed the P4 at (284.5, 119.5)
- removed the P4 at (308.5, 119.5)
- removed the P4 at (304.5, 119.5)
- removed the P4 at (300.5, 119.5)
- removed the P4 at (296.5, 119.5)
- removed the P4 at (292.5, 119.5)
- removed the P4 at (372.5, 119.5)
- removed the P4 at (376.5, 119.5)
- removed the P4 at (368.5, 119.5)
- removed the P4 at (364.5, 119.5)
- removed the P4 at (360.5, 119.5)
- removed the P4 at (356.5, 119.5)
- removed the P4 at (352.5, 119.5)
- removed the P5 at (288.5, 116.5)
- removed the P5 at (328.5, 116.5)
- removed the P5 at (312.5, 116.5)
- removed the P5 at (316.5, 116.5)
- removed the P5 at (324.5, 116.5)
- removed the P5 at (320.5, 116.5)
- removed the P5 at (360.5, 116.5)
- removed the P5 at (364.5, 116.5)
- removed the P5 at (356.5, 116.5)
- removed the P5 at (352.5, 116.5)
- removed the P5 at (368.5, 116.5)
- removed the P5 at (284.5, 116.5)
- removed the P5 at (348.5, 116.5)
- removed the P5 at (332.5, 116.5)
- removed the P5 at (336.5, 116.5)
- removed the P5 at (344.5, 116.5)
- removed the P5 at (340.5, 116.5)
- removed the P5 at (372.5, 116.5)
- removed the P5 at (376.5, 116.5)
- removed the P5 at (300.5, 116.5)
- removed the P5 at (304.5, 116.5)
- removed the P5 at (296.5, 116.5)
- removed the P5 at (292.5, 116.5)
- removed the P5 at (308.5, 116.5)
- removed the P6 at (288.5, 89.5)
- removed the P6 at (328.5, 89.5)
- removed the P6 at (312.5, 89.5)
- removed the P6 at (316.5, 89.5)
- removed the P6 at (324.5, 89.5)
- removed the P6 at (320.5, 89.5)
- removed the P6 at (360.5, 89.5)
- removed the P6 at (364.5, 89.5)
- removed the P6 at (356.5, 89.5)
- removed the P6 at (352.5, 89.5)
- removed the P6 at (368.5, 89.5)
- removed the P6 at (284.5, 89.5)
- removed the P6 at (348.5, 89.5)
- removed the P6 at (332.5, 89.5)
- removed the P6 at (336.5, 89.5)
- removed the P6 at (344.5, 89.5)
- removed the P6 at (340.5, 89.5)
- removed the P6 at (372.5, 89.5)
- removed the P6 at (376.5, 89.5)
- removed the P6 at (300.5, 89.5)
- removed the P6 at (304.5, 89.5)
- removed the P6 at (296.5, 89.5)
- removed the P6 at (292.5, 89.5)
- removed the P6 at (308.5, 89.5)
- removed the P7 at (288.5, 89.5)
- removed the P7 at (328.5, 89.5)
- removed the P7 at (312.5, 89.5)
- removed the P7 at (316.5, 89.5)
- removed the P7 at (324.5, 89.5)
- removed the P7 at (320.5, 89.5)
- removed the P7 at (360.5, 89.5)
- removed the P7 at (364.5, 89.5)
- removed the P7 at (356.5, 89.5)
- removed the P7 at (352.5, 89.5)
- removed the P7 at (368.5, 89.5)
- removed the P7 at (284.5, 89.5)
- removed the P7 at (348.5, 89.5)
- removed the P7 at (332.5, 89.5)
- removed the P7 at (336.5, 89.5)
- removed the P7 at (344.5, 89.5)
- removed the P7 at (340.5, 89.5)
- removed the P7 at (372.5, 89.5)
- removed the P7 at (376.5, 89.5)
- removed the P7 at (300.5, 89.5)
- removed the P7 at (304.5, 89.5)
- removed the P7 at (296.5, 89.5)
- removed the P7 at (292.5, 89.5)
- removed the P7 at (308.5, 89.5)
- removed the P8 at (288.5, 116.5)
- removed the P8 at (328.5, 116.5)
- removed the P8 at (312.5, 116.5)
- removed the P8 at (316.5, 116.5)
- removed the P8 at (324.5, 116.5)
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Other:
- board text added: "2014 V0.20.b"
- board text removed: "2014 V0.20.a"
